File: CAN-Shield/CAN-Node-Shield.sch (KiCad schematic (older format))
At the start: 22 parts, among them J1 Main_Port_1, J10 IOH, J2 Main_Port_2, J3 Sensor, J4 Sensor, J5 Sensor, J6 Sensor, J7 Power, J8 Analog, J9 IOL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

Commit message: CAN terminating resistor change
I updated the layout to include options for both High-speed CAN and Low-speed CAN terminating resistor configurations. There are positions for either type of termination so the board can be used for either bus type.
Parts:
- added R2: 500, Resistor_THT:R_Axial_DIN0207_L6.3mm_D2.5mm_P10.16mm_Horizontal, symbol Device:R
- added R4: 120, Resistor_THT:R_Axial_DIN0207_L6.3mm_D2.5mm_P10.16mm_Horizontal, symbol Device:R
- R1: value 120 -> 500
- renumbered R2 to R3
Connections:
- net +5V: now also R2.2
- net GND: now also R1.2
- net at J1.4 (CANH), J2.4 (CANH), R1.1: now also U1.7 (CANH), R4.2; no longer U1.6 (CANL)
- net at J1.3 (CANL), J2.3 (CANL): now also U1.6 (CANL), R2.1, R4.1; no longer R1.2, U1.7 (CANH)
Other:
- moved on the sheet: J1, J2, R1
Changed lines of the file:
@@
 L CAN-Node-Shield-rescue:Main_Port-CAN-Node-Shield-cache J1
 U 1 1 6051E7E9
-P 800 2250
-F 0 "J1" H 1008 2825 50  0000 C CNN
-F 1 "Main_Port_1" H 1008 2734 50  0000 C CNN
-F 2 "Connector_PinHeader_2.54mm:PinHeader_1x04_P2.54mm_Vertical" H 850 2100 50  0001 C CNN
-F 3 "" H 850 2100 50  0001 C CNN
-	1    800  2250
+P 750 2450
+F 0 "J1" H 958 3025 50  0000 C CNN
+F 1 "Main_Port_1" H 958 2934 50  0000 C CNN
+F 2 "Connector_PinHeader_2.54mm:PinHeader_1x04_P2.54mm_Vertical" H 800 2300 50  0001 C CNN
+F 3 "" H 800 2300 50  0001 C CNN
+	1    750  2450
 	1    0    0    -1
 $EndComp
@@
 L Device:R R1
 U 1 1 605323AC
-P 2000 2250
-F 0 "R1" H 1930 2204 50  0000 R CNN
-F 1 "120" H 1930 2295 50  0000 R CNN
-F 2 "Resistor_THT:R_Axial_DIN0207_L6.3mm_D2.5mm_P10.16mm_Horizontal" V 1930 2250 50  0001 C CNN
-F 3 "~" H 2000 2250 50  0001 C CNN
-	1    2000 2250
+P 2000 1950
+F 0 "R1" H 1930 1904 50  0000 R CNN
+F 1 "500" H 1930 1995 50  0000 R CNN
+F 2 "Resistor_THT:R_Axial_DIN0207_L6.3mm_D2.5mm_P10.16mm_Horizontal" V 1930 1950 50  0001 C CNN
+F 3 "~" H 2000 1950 50  0001 C CNN
+	1    2000 1950
 	-1   0    0    1
 $EndComp
 Wire Wire Line
-	2550 2100 2000 2100
-Wire Wire Line
-	1700 2200 1700 2400
-Wire Wire Line
-	2300 2400 2300 2300
-Wire Wire Line
-	2300 2300 2550 2300
-Connection ~ 2000 2100
-Connection ~ 2000 2400
-Wire Wire Line
-	2000 2400 2300 2400
-Wire Wire Line
-	1700 2400 2000 2400
+	2550 2100 2250 2100
 $Comp
 L power:GND #PWR02
 U 1 1 60534CEE
-P 1700 1850
-F 0 "#PWR02" H 1700 1600 50  0001 C CNN
-F 1 "GND" H 1705 1677 50  0000 C CNN
-F 2 "" H 1700 1850 50  0001 C CNN
-F 3 "" H 1700 1850 50  0001 C CNN
-	1    1700 1850
-	1    0    0    -1
-$EndComp
-Wire Wire Line
-	1550 1800 1550 2000
+P 1650 2050
+F 0 "#PWR02" H 1650 1800 50  0001 C CNN
+F 1 "GND" H 1655 1877 50  0000 C CNN
+F 2 "" H 1650 2050 50  0001 C CNN
+F 3 "" H 1650 2050 50  0001 C CNN
+	1    1650 2050
+	1    0    0    -1
+$EndComp
+Wire Wire Line
+	1500 2000 1500 2200
 $Comp
 L power:+12V #PWR01
 U 1 1 60535F1B
-P 1700 1550
-F 0 "#PWR01" H 1700 1400 50  0001 C CNN
-F 1 "+12V" H 1715 1723 50  0000 C CNN
-F 2 "" H 1700 1550 50  0001 C CNN
-F 3 "" H 1700 1550 50  0001 C CNN
-	1    1700 1550
-	1    0    0    -1
-$EndComp
-Wire Wire Line
-	1700 1600 1700 1550
-Wire Wire Line
-	1700 1600 1450 1600
-Wire Wire Line
-	1450 1600 1450 1900
-$Comp
-L power:+12V #PWR026
+P 1650 1750
+F 0 "#PWR01" H 1650 1600 50  0001 C CNN
+F 1 "+12V" H 1665 1923 50  0000 C CNN
+F 2 "" H 1650 1750 50  0001 C CNN
+F 3 "" H 1650 1750 50  0001 C CNN
+	1    1650 1750
+	1    0    0    -1
+$EndComp
+Wire Wire Line
+	1650 1800 1650 1750
+Wire Wire Line
+	1650 1800 1400 1800
+Wire Wire Line
+	1400 1800 1400 2100
+$Comp
+L power:+12V #PWR025
 U 1 1 60537867
 P 9700 1050
-F 0 "#PWR026" H 9700 900 50  0001 C CNN
+F 0 "#PWR025" H 9700 900 50  0001 C CNN
 F 1 "+12V" H 9715 1223 50  0000 C CNN
 F 2 "" H 9700 1050 50  0001 C CNN
@@
 $EndComp
 $Comp
-L power:+5V #PWR025
+L power:+5V #PWR024
 U 1 1 60539615
 P 9400 1350
-F 0 "#PWR025" H 9400 1200 50  0001 C CNN
+F 0 "#PWR024" H 9400 1200 50  0001 C CNN
 F 1 "+5V" H 9415 1523 50  0000 C CNN
 F 2 "" H 9400 1350 50  0001 C CNN
@@
 	7650 5200 9100 5200
 $Comp
-L power:GND #PWR024
+L power:GND #PWR026
 U 1 1 6053816E
 P 9700 1400
-F 0 "#PWR024" H 9700 1150 50  0001 C CNN
+F 0 "#PWR026" H 9700 1150 50  0001 C CNN
 F 1 "GND" H 9705 1227 50  0000 C CNN
 F 2 "" H 9700 1400 50  0001 C CNN
@@
 	2550 6600 2550 6650
 $Comp
-L power:+5V #PWR010
+L power:+5V #PWR07
 U 1 1 605A9E04
 P 2550 6600
-F 0 "#PWR010" H 2550 6450 50  0001 C CNN
+F 0 "#PWR07" H 2550 6450 50  0001 C CNN
 F 1 "+5V" H 2565 6773 50  0000 C CNN
 F 2 "" H 2550 6600 50  0001 C CNN
@@
 	2550 5850 2550 5900
 $Comp
-L power:+5V #PWR08
+L power:+5V #PWR06
 U 1 1 605A8178
 P 2550 5850
-F 0 "#PWR08" H 2550 5700 50  0001 C CNN
+F 0 "#PWR06" H 2550 5700 50  0001 C CNN
 F 1 "+5V" H 2565 6023 50  0000 C CNN
 F 2 "" H 2550 5850 50  0001 C CNN
@@
 	2550 5900 2450 5900
 $Comp
-L power:GND #PWR09
+L power:GND #PWR010
 U 1 1 605A8170
 P 2800 5850
-F 0 "#PWR09" H 2800 5600 50  0001 C CNN
+F 0 "#PWR010" H 2800 5600 50  0001 C CNN
 F 1 "GND" H 2805 5677 50  0000 C CNN
 F 2 "" H 2800 5850 50  0001 C CNN
@@
 	2550 5100 2550 5150
 $Comp
-L power:+5V #PWR06
+L power:+5V #PWR05
 U 1 1 605A69A3
 P 2550 5100
-F 0 "#PWR06" H 2550 4950 50  0001 C CNN
+F 0 "#PWR05" H 2550 4950 50  0001 C CNN
 F 1 "+5V" H 2565 5273 50  0000 C CNN
 F 2 "" H 2550 5100 50  0001 C CNN
@@
 	2550 5150 2450 5150
 $Comp
-L power:GND #PWR07
+L power:GND #PWR09
 U 1 1 605A699B
 P 2800 5100
-F 0 "#PWR07" H 2800 4850 50  0001 C CNN
+F 0 "#PWR09" H 2800 4850 50  0001 C CNN
 F 1 "GND" H 2805 4927 50  0000 C CNN
 F 2 "" H 2800 5100 50  0001 C CNN
@@
 	2550 4400 2450 4400
 $Comp
-L power:GND #PWR05
+L power:GND #PWR08
 U 1 1 605553DF
 P 2800 4350
-F 0 "#PWR05" H 2800 4100 50  0001 C CNN
+F 0 "#PWR08" H 2800 4100 50  0001 C CNN
 F 1 "GND" H 2805 4177 50  0000 C CNN
 F 2 "" H 2800 4350 50  0001 C CNN
@@
 	9800 4800 9800 5700
 Wire Wire Line
-	1200 1900 1250 1900
-Wire Wire Line
-	1250 1900 1250 2800
-Connection ~ 1250 1900
-Wire Wire Line
-	1250 1900 1450 1900
-Wire Wire Line
-	1350 2000 1350 2900
-Wire Wire Line
-	1450 2100 1450 3000
-Wire Wire Line
-	1550 2200 1550 3100
-Connection ~ 1550 2200
-Wire Wire Line
-	1550 2200 1700 2200
-Wire Wire Line
-	1200 2200 1550 2200
-Connection ~ 1450 2100
-Wire Wire Line
-	1450 2100 2000 2100
-Wire Wire Line
-	1200 2100 1450 2100
-Connection ~ 1350 2000
-Wire Wire Line
-	1200 2000 1350 2000
-Wire Wire Line
-	1550 1800 1700 1800
-Wire Wire Line
-	1350 2000 1550 2000
+	1150 2100 1200 2100
+Wire Wire Line
+	1200 2100 1200 3000
+Connection ~ 1200 2100
+Wire Wire Line
+	1200 2100 1400 2100
+Wire Wire Line
+	1300 2200 1300 3100
+Connection ~ 1300 2200
+Wire Wire Line
+	1150 2200 1300 2200
+Wire Wire Line
+	1500 2000 1650 2000
+Wire Wire Line
+	1300 2200 1500 2200
 $Comp
 L CAN-Node-Shield-rescue:Main_Port-CAN-Node-Shield-cache J2
 U 1 1 6061F6EF
-P 800 3150
-F 0 "J2" H 1008 3725 50  0000 C CNN
-F 1 "Main_Port_2" H 1008 3634 50  0000 C CNN
-F 2 "Connector_PinHeader_2.54mm:PinHeader_1x04_P2.54mm_Vertical" H 850 3000 50  0001 C CNN
-F 3 "" H 850 3000 50  0001 C CNN
-	1    800  3150
-	1    0    0    -1
-$EndComp
-Wire Wire Line
-	1200 2800 1250 2800
-Wire Wire Line
-	1200 2900 1350 2900
-Wire Wire Line
-	1200 3000 1450 3000
-Wire Wire Line
-	1200 3100 1550 3100
+P 750 3350
+F 0 "J2" H 958 3925 50  0000 C CNN
+F 1 "Main_Port_2" H 958 3834 50  0000 C CNN
+F 2 "Connector_PinHeader_2.54mm:PinHeader_1x04_P2.54mm_Vertical" H 800 3200 50  0001 C CNN
+F 3 "" H 800 3200 50  0001 C CNN
+	1    750  3350
+	1    0    0    -1
+$EndComp
+Wire Wire Line
+	1150 3000 1200 3000
+Wire Wire Line
+	1150 3100 1300 3100
+Wire Wire Line
+	1150 3200 1400 3200
+Wire Wire Line
+	1150 3300 1500 3300
 $Comp
 L power:+5V #PWR015
@@
 $EndComp
 $Comp
-L Device:R R2
+L Device:R R3
 U 1 1 6070D84F
 P 5500 6850
-F 0 "R2" V 5300 6850 50  0000 R CNN
+F 0 "R3" V 5300 6850 50  0000 R CNN
 F 1 "120" V 5400 6900 50  0000 R CNN
 F 2 "Resistor_THT:R_Axial_DIN0207_L6.3mm_D2.5mm_P10.16mm_Horizontal" V 5430 6850 50  0001 C CNN
@@
 	3050 2700 3050 2800
 Wire Wire Line
-	1700 1800 1700 1850
+	1650 2000 1650 2050
 $Comp
 L 2021-03-16_21-10-04:C0805C200G8HAC7800 C1
@@
 Wire Wire Line
 	2650 6550 2800 6550
+$Comp
+L Device:R R2
+U 1 1 60883E2D
+P 2150 2700
+F 0 "R2" H 2080 2654 50  0000 R CNN
+F 1 "500" H 2080 2745 50  0000 R CNN
+F 2 "Resistor_THT:R_Axial_DIN0207_L6.3mm_D2.5mm_P10.16mm_Horizontal" V 2080 2700 50  0001 C CNN
+F 3 "~" H 2150 2700 50  0001 C CNN
+	1    2150 2700
+	1    0    0    -1
+$EndComp
+$Comp
+L power:GND #PWR0101
+U 1 1 6088C69C
+P 2350 1850
+F 0 "#PWR0101" H 2350 1600 50  0001 C CNN
+F 1 "GND" H 2355 1677 50  0000 C CNN
+F 2 "" H 2350 1850 50  0001 C CNN
+F 3 "" H 2350 1850 50  0001 C CNN
+	1    2350 1850
+	1    0    0    -1
+$EndComp
+Wire Wire Line
+	2350 1800 2350 1850
+Wire Wire Line
+	2000 1800 2350 1800
+$Comp
+L power:+5V #PWR0102
+U 1 1 6089D221
+P 1800 2850
+F 0 "#PWR0102" H 1800 2700 50  0001 C CNN
+F 1 "+5V" H 1815 3023 50  0000 C CNN
+F 2 "" H 1800 2850 50  0001 C CNN
+F 3 "" H 1800 2850 50  0001 C CNN
+	1    1800 2850
+	1    0    0    -1
+$EndComp
+Wire Wire Line
+	1150 2300 1400 2300
+Wire Wire Line
+	1400 3200 1400 2300
+Connection ~ 1400 2300
+Wire Wire Line
+	1400 2300 2150 2300
+Wire Wire Line
+	1150 2400 1500 2400
+Wire Wire Line
+	2000 2400 2000 2100
+Connection ~ 2000 2100
+Wire Wire Line
+	1500 3300 1500 2400
+Connection ~ 1500 2400
+Wire Wire Line
+	1500 2400 2000 2400
+Wire Wire Line
+	2150 2550 2150 2300
+Connection ~ 2150 2300
+Wire Wire Line
+	2150 2300 2550 2300
+Wire Wire Line
+	1800 2850 2150 2850
+$Comp
+L Device:R R4
+U 1 1 609BE8BB
+P 2400 2450
+F 0 "R4" V 2200 2450 50  0000 R CNN
+F 1 "120" V 2300 2500 50  0000 R CNN
+F 2 "Resistor_THT:R_Axial_DIN0207_L6.3mm_D2.5mm_P10.16mm_Horizontal" V 2330 2450 50  0001 C CNN
+F 3 "~" H 2400 2450 50  0001 C CNN
+	1    2400 2450
+	0    1    1    0
+$EndComp
+Wire Wire Line
+	2250 2450 2250 2100
+Connection ~ 2250 2100
+Wire Wire Line
+	2250 2100 2000 2100
+Wire Wire Line
+	2550 2450 2550 2300
+Connection ~ 2550 2300
 $EndSCHEMATC

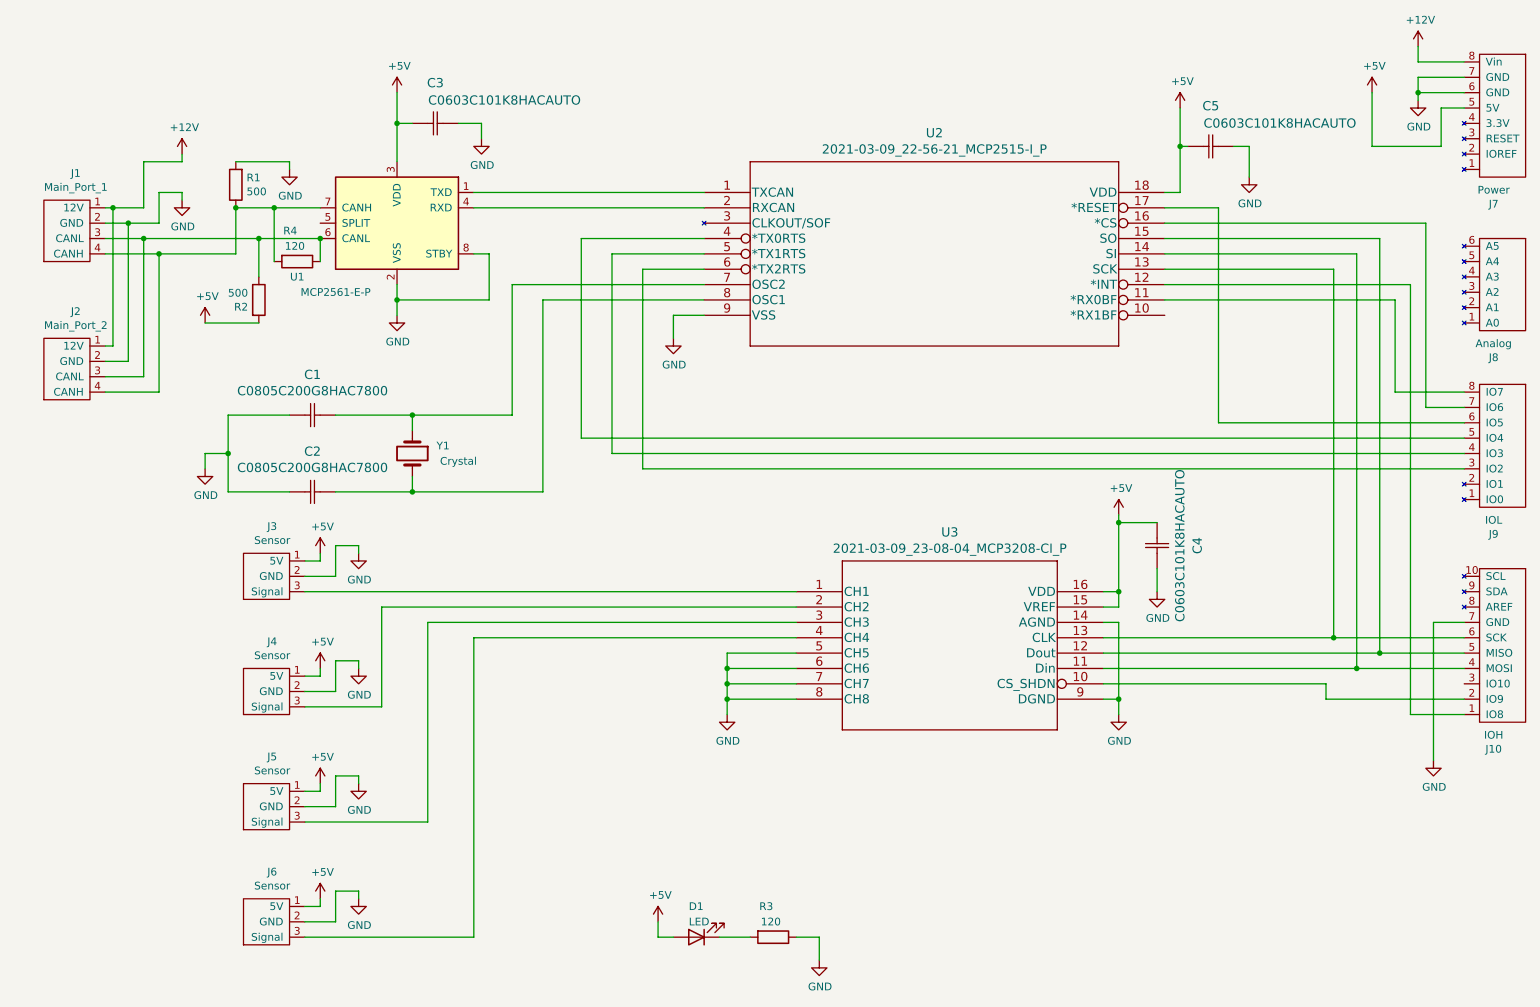
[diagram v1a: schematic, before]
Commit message: Informational silkscreen and new board footprint
Changes made:
 - Adjusted bottom two Arduino headers; they were too far to the left by 2mm
 - Added silkscreen labels to header pins for easy identification of pin function
 - Reduced board footprint to allow for smaller enclosures
 - Chamfered corners to prevent them from being too pointy
 - Added my name :)
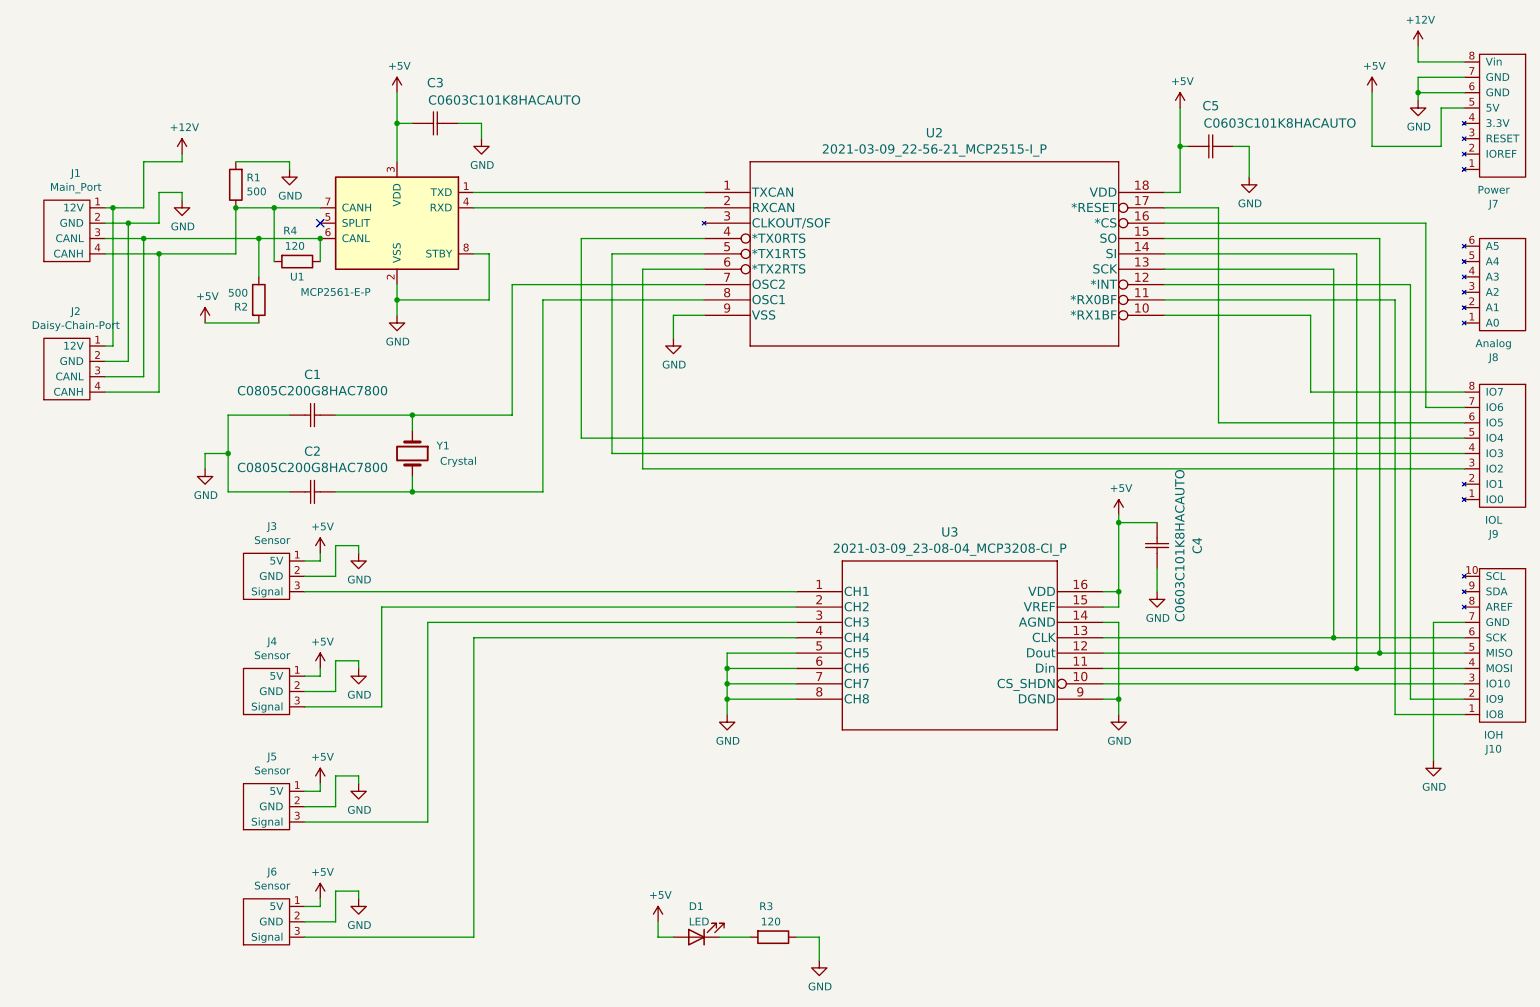
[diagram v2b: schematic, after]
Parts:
- removed J2: Main_Port_2, Connector_PinHeader_2.54mm:PinHeader_1x04_P2.54mm_Vertical, symbol CAN-Node-Shield-rescue:Main_Port-CAN-Node-Shield-cache
- added J2: Daisy-Chain-Port, Connector_PinHeader_2.54mm:PinHeader_1x04_P2.54mm_Vertical, symbol CAN-Node-Shield-rescue:Daisy-Chain-Port
- J1: value Main_Port_1 -> Main_Port
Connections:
- net +12V: now also J2.1 (12V)
- net GND: now also J2.2 (GND)
- net at J1.3 (CANL), R2.1, R4.1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: now also J2.3 (CANL)
- net at J1.4 (CANH), R1.1, R4.2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: now also J2.4 (CANH)
- net at J9.8 (IO7): now also U2.10 (*RX1BF); no longer U2.11 (*RX0BF)
- net at J10.1 (IO8): now also U2.11 (*RX0BF); no longer U2.12 (*INT)
- net at J10.2 (IO9): now also U2.12 (*INT); no longer U3.10 (CS_SHDN)
- net at J10.3 (IO10): now also U3.10 (CS_SHDN)
- no-connect marks 0 -> 1
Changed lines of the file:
@@
 P 750 2450
 F 0 "J1" H 958 3025 50  0000 C CNN
-F 1 "Main_Port_1" H 958 2934 50  0000 C CNN
+F 1 "Main_Port" H 958 2934 50  0000 C CNN
 F 2 "Connector_PinHeader_2.54mm:PinHeader_1x04_P2.54mm_Vertical" H 800 2300 50  0001 C CNN
 F 3 "" H 800 2300 50  0001 C CNN
@@
 	1    0    0    -1
 $EndComp
-Wire Wire Line
-	7650 5200 9100 5200
 $Comp
 L power:GND #PWR026
@@
 Wire Wire Line
 	1300 2200 1500 2200
-$Comp
-L CAN-Node-Shield-rescue:Main_Port-CAN-Node-Shield-cache J2
-U 1 1 6061F6EF
-P 750 3350
-F 0 "J2" H 958 3925 50  0000 C CNN
-F 1 "Main_Port_2" H 958 3834 50  0000 C CNN
-F 2 "Connector_PinHeader_2.54mm:PinHeader_1x04_P2.54mm_Vertical" H 800 3200 50  0001 C CNN
-F 3 "" H 800 3200 50  0001 C CNN
-	1    750  3350
-	1    0    0    -1
-$EndComp
 Wire Wire Line
 	1150 3000 1200 3000
@@
 	9750 3400 10000 3400
 Wire Wire Line
-	9100 5200 9100 5300
-Wire Wire Line
-	9100 5300 10000 5300
-Wire Wire Line
-	9550 2700 9550 3300
-Wire Wire Line
-	9650 5400 10000 5400
-Wire Wire Line
-	9650 2600 9650 5400
-Wire Wire Line
-	10000 3300 9550 3300
-Wire Wire Line
-	2450 4500 2650 4500
+	9650 2600 9650 5300
 Wire Wire Line
 	2650 4500 2650 4300
@@
 	2550 2450 2550 2300
 Connection ~ 2550 2300
+NoConn ~ 2550 2200
+Wire Wire Line
+	2650 4500 2450 4500
+$Comp
+L CAN-Node-Shield-rescue:Daisy-Chain-Port J2
+U 1 1 60AC3410
+P 750 3350
+F 0 "J2" H 958 3925 50  0000 C CNN
+F 1 "Daisy-Chain-Port" H 958 3834 50  0000 C CNN
+F 2 "Connector_PinHeader_2.54mm:PinHeader_1x04_P2.54mm_Vertical" H 800 3200 50  0001 C CNN
+F 3 "" H 800 3200 50  0001 C CNN
+	1    750  3350
+	1    0    0    -1
+$EndComp
+Wire Wire Line
+	8050 2800 9000 2800
+Wire Wire Line
+	7650 5200 10000 5200
+Wire Wire Line
+	10000 5300 9650 5300
+Wire Wire Line
+	9550 2700 9550 5400
+Wire Wire Line
+	9550 5400 10000 5400
+Wire Wire Line
+	9000 2800 9000 3300
+Wire Wire Line
+	9000 3300 10000 3300
 $EndSCHEMATC
